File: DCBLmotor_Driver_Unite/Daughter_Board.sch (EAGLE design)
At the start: 46 parts, among them CN2 DF63-2P-3.96DSA, CN4 DF63-3P-3.96DSA, IC1 IR25750LPBF, IC2 IR25750LPBF, IC3 IR25750LPBF, IC4 DRV8320SRTVT, IC6 LTM8050IY#PBF-ND, IC7 TMPM373FWDUG

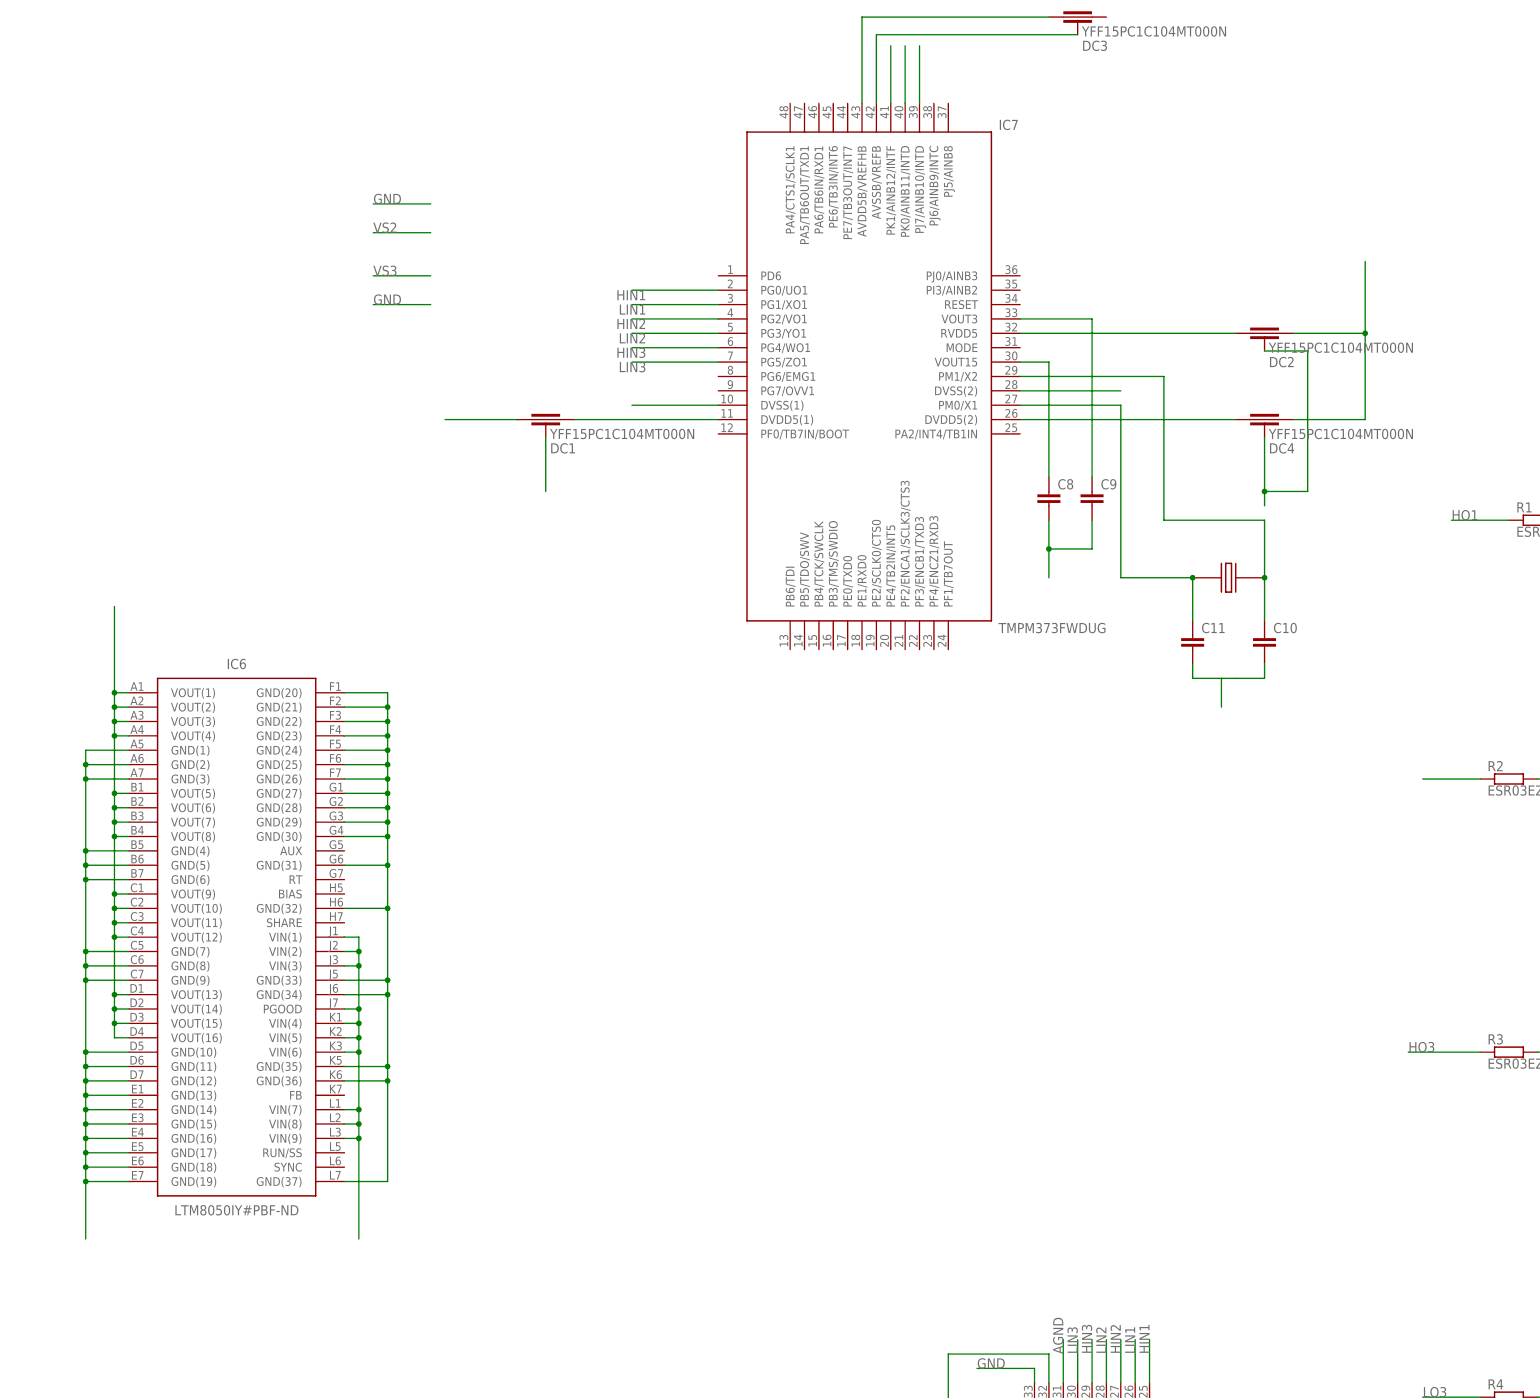
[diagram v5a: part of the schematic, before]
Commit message: Attach DC-DC Converter
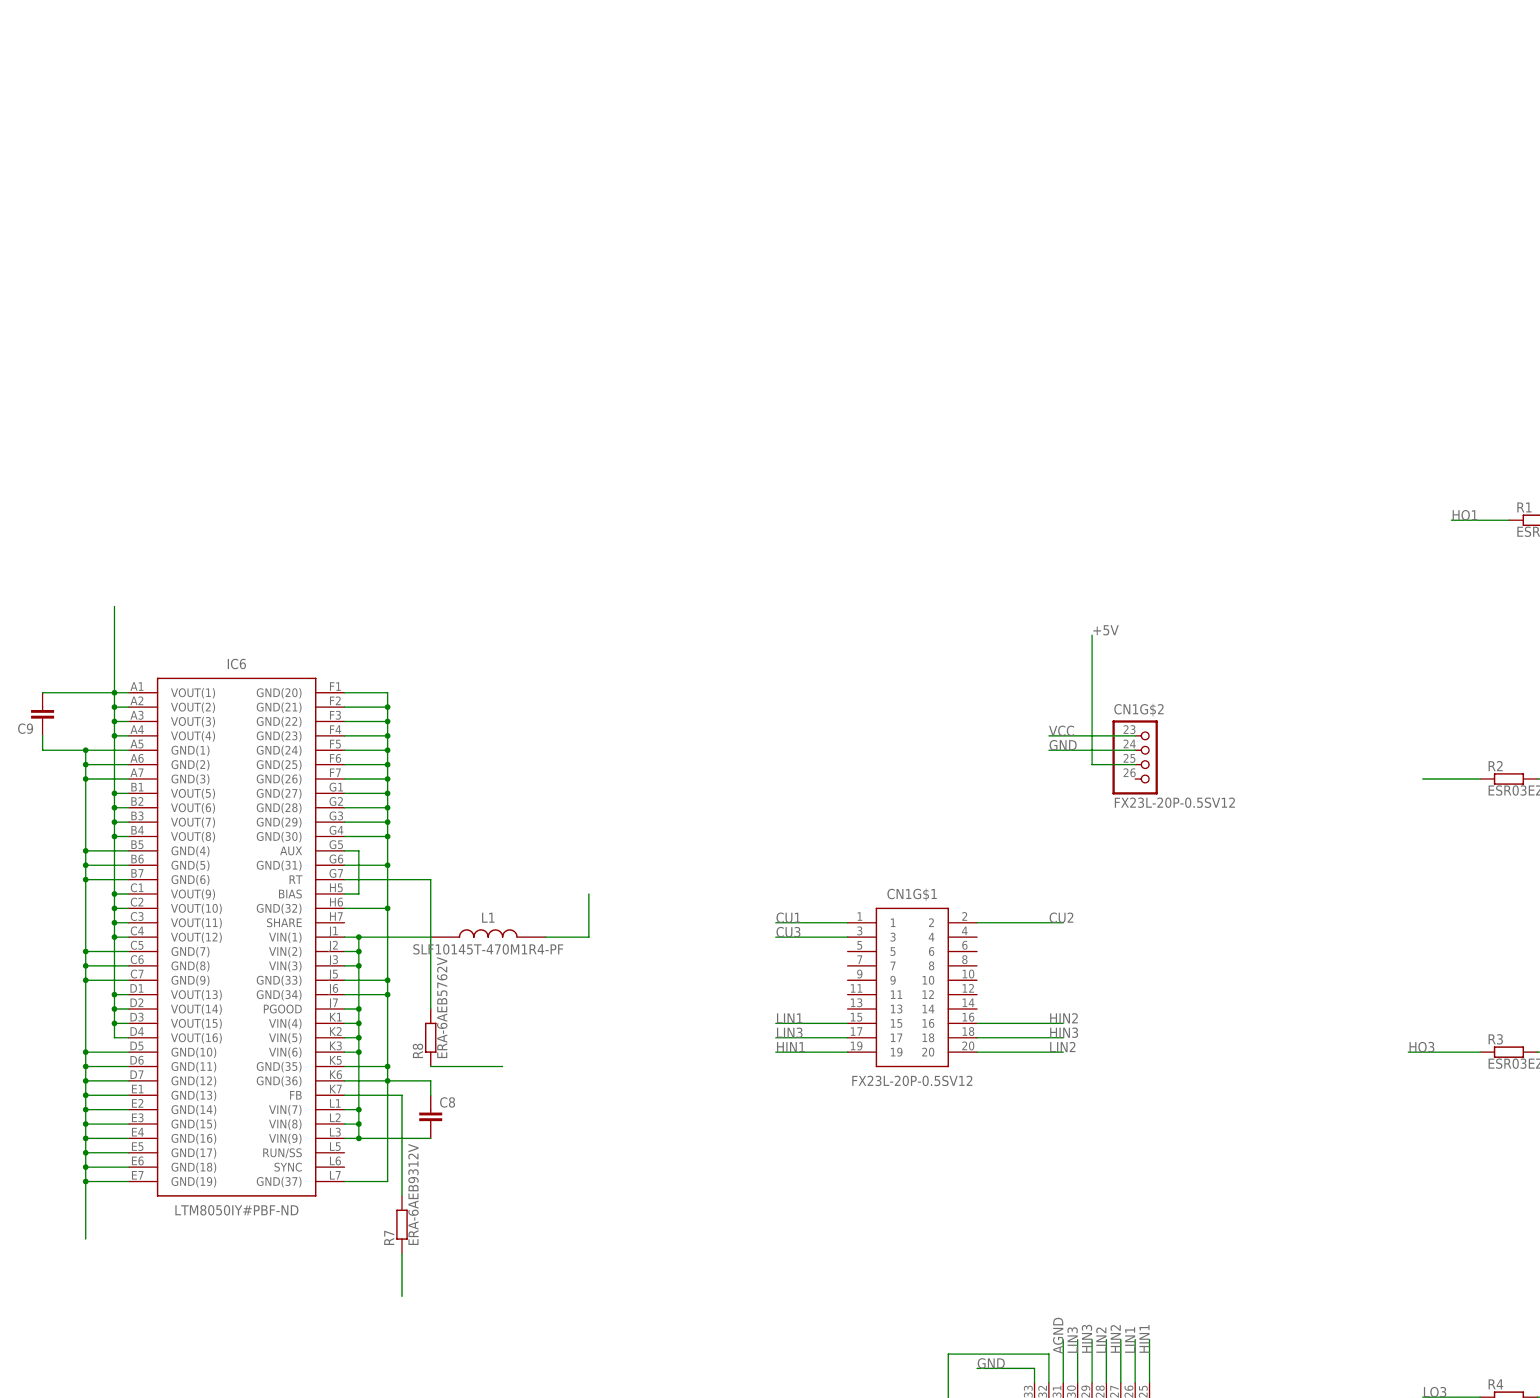
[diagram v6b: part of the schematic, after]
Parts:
- removed C10, C11: GRM0225C1E120JA03L, murata:GRM0225C1E120JA03L
- removed DC1, DC2, DC3, DC4: YFF15PC1C104MT000N, TDK:YFF15PC1C104MT000N
- removed IC7: TMPM373FWDUG, TMPM373FWDUG:TMPM373FWDUG
- removed XTAL1: ABM8AIG-10.000MHZ-12-2Z-T3, Abracon:ABM8AIG-10.000MHZ-12-2Z-T3
- added CN1: FX23L-20P-0.5SV12, FX23L-20P-0.5SV12:FX23L-20P-0.5SV12
- added L1: SLF10145T-470M1R4-PF, TDK:SLF10145T-470M1R4-PF
- added R7: ERA-6AEB9312V, Panasonic:ERA-6AEB9312V
- added R8: ERA-6AEB5762V, Panasonic:ERA-6AEB5762V
- C8: value GRM035R60J475ME15D -> CGA6M3X7S2A475M200AB; device murata:GRM035R60J475ME15D -> TDK:CGA6M3X7S2A475M200AB
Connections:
- removed net N$10: DC1.P$2, IC7.DVDD5(1)
- removed net N$11: DC3.P$1, IC7.AVDD5B/VREFHB
- removed net N$12: DC3.GND, IC7.AVSSB/VREFB
- removed net N$13: C8.1, IC7.VOUT15
- removed net N$14: C9.1, IC7.VOUT3
- removed net N$9: DC4.P$1, IC7.DVDD5(2)
- new net +5V: C9.2, CN1G$2.3, IC6.VOUT(1), IC6.VOUT(10), IC6.VOUT(11), IC6.VOUT(12), IC6.VOUT(13), IC6.VOUT(14), IC6.VOUT(15), IC6.VOUT(16), IC6.VOUT(2), IC6.VOUT(3), IC6.VOUT(4), IC6.VOUT(5), IC6.VOUT(6), IC6.VOUT(7), IC6.VOUT(8), IC6.VOUT(9)
- new net IN_A: C8.2, IC6.PGOOD, IC6.VIN(1), IC6.VIN(2), IC6.VIN(3), IC6.VIN(4), IC6.VIN(5), IC6.VIN(6), IC6.VIN(7), IC6.VIN(8), IC6.VIN(9), L1.1
- net +3.3V: no longer DC1.P$1, DC2.P$2, DC4.P$2, IC6.VOUT(1), IC6.VOUT(10), IC6.VOUT(11), IC6.VOUT(12), IC6.VOUT(13), IC6.VOUT(14), IC6.VOUT(15), IC6.VOUT(16), IC6.VOUT(2), IC6.VOUT(3), IC6.VOUT(4), IC6.VOUT(5), IC6.VOUT(6), IC6.VOUT(7), IC6.VOUT(8), IC6.VOUT(9)
- net CU1: now also CN1G$1.1; no longer IC7.PJ7/AINB10/INTD
- net CU2: now also CN1G$1.2; no longer IC7.PK0/AINB11/INTD
- net CU3: now also CN1G$1.3; no longer IC7.PK1/AINB12/INTF
- net GND: now also C8.1, C9.1, CN1G$2.2, R7.2, R8.2; no longer C10.2, C11.2, C8.2, C9.2, DC1.GND, DC2.GND, DC4.GND, IC7.DVSS(1), IC7.DVSS(2)
- net HIN1: now also CN1G$1.19; no longer IC7.PG0/UO1
- net HIN2: now also CN1G$1.16; no longer IC7.PG2/VO1
- net HIN3: now also CN1G$1.18; no longer IC7.PG4/WO1
- net LIN1: now also CN1G$1.15; no longer IC7.PG1/XO1
- net LIN2: now also CN1G$1.20; no longer IC7.PG3/YO1
- net LIN3: now also CN1G$1.17; no longer IC7.PG5/ZO1
- net N$1: now also IC6.AUX, IC6.BIAS; no longer C10.1, IC7.PM1/X2, XTAL1.P$1
- net N$3: now also IC6.FB, R7.1; no longer C11.1, IC7.PM0/X1, XTAL1.P$2
- net N$6: now also IC6.RT, R8.1; no longer DC2.P$1, IC7.RVDD5
- net VCC: now also CN1G$2.1, L1.2; no longer IC6.PGOOD, IC6.VIN(1), IC6.VIN(2), IC6.VIN(3), IC6.VIN(4), IC6.VIN(5), IC6.VIN(6), IC6.VIN(7), IC6.VIN(8), IC6.VIN(9)
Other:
- moved on the sheet: C8, C9

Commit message: Change to 1 shant
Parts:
- removed IC2, IC3: IR25750LPBF, Infinion:IR25750LPBF
- IC1: value IR25750LPBF -> ACS780KLRTR-150B-T; device Infinion:IR25750LPBF -> ACS780:ACS780KLRTR-150B-T
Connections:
- new net LOSIDE: C4.2, C5.2, C6.2, FD2.A, FD4.A, FD6.A, FET2.S, FET4.S, FET6.S, IC1.IP+, IC4.SLA, IC4.SLB, IC4.SLC, PMC1.2, PMC2.2, PMC3.2
- net CU1: now also IC1.VOUT; no longer IC1.CS
- net CU2: no longer IC2.CS
- net CU3: no longer IC3.CS
- net GND: now also IC1.IP-; no longer C4.2, C5.2, C6.2, FD2.A, FD4.A, FD6.A, FET2.S, FET4.S, FET6.S, IC1.COM, IC2.COM, IC3.COM, IC4.SLA, IC4.SLB, IC4.SLC, PMC1.2, PMC2.2, PMC3.2
- net N$18: no longer IC3.GATE
- net N$2: no longer IC2.GATE
- net N$4: no longer IC1.GATE
- net VS1: no longer IC1.VS
- net VS2: no longer IC2.VS
- net VS3: no longer IC3.VS

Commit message: Main_borad is Almost_finshed
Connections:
- removed net AGND: C2.1, IC4.AGND, IC4.PGND
- net GND: now also C2.1, IC4.AGND, IC4.PGND
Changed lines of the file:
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@@
 <wire x1="-165.1" y1="7.62" x2="-152.4" y2="7.62" width="0.1524" layer="91"/>
+</segment>
+<segment>
+<pinref part="C2" gate="G$1" pin="1"/>
+<wire x1="-27.94" y1="-68.58" x2="-27.94" y2="-76.2" width="0.1524" layer="91"/>
+<pinref part="IC4" gate="G$1" pin="AGND"/>
+<wire x1="-27.94" y1="-76.2" x2="-30.48" y2="-76.2" width="0.1524" layer="91"/>
+<wire x1="-27.94" y1="-76.2" x2="-17.78" y2="-76.2" width="0.1524" layer="91"/>
+<junction x="-27.94" y="-76.2"/>
+<label x="-20.32" y="-76.2" size="1.778" layer="95"/>
+</segment>
+<segment>
+<pinref part="IC4" gate="G$1" pin="PGND"/>
+<wire x1="-53.34" y1="-48.26" x2="-53.34" y2="-40.64" width="0.1524" layer="91"/>
+<label x="-53.34" y="-43.18" size="1.778" layer="95" rot="R90"/>
 </segment>
 </net>
@@
 </segment>
 </net>
-<net name="AGND" class="0">
-<segment>
-<pinref part="C2" gate="G$1" pin="1"/>
-<wire x1="-27.94" y1="-68.58" x2="-27.94" y2="-76.2" width="0.1524" layer="91"/>
-<pinref part="IC4" gate="G$1" pin="AGND"/>
-<wire x1="-27.94" y1="-76.2" x2="-30.48" y2="-76.2" width="0.1524" layer="91"/>
-</segment>
-<segment>
-<pinref part="IC4" gate="G$1" pin="PGND"/>
-<wire x1="-53.34" y1="-48.26" x2="-53.34" y2="-40.64" width="0.1524" layer="91"/>
-<label x="-53.34" y="-43.18" size="1.778" layer="95" rot="R90"/>
-</segment>
-</net>
